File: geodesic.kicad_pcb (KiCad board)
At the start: 2 copper layers, 127.7 x 130 mm, 12 parts, among them J2 Base, U1 ATtiny24A-MU

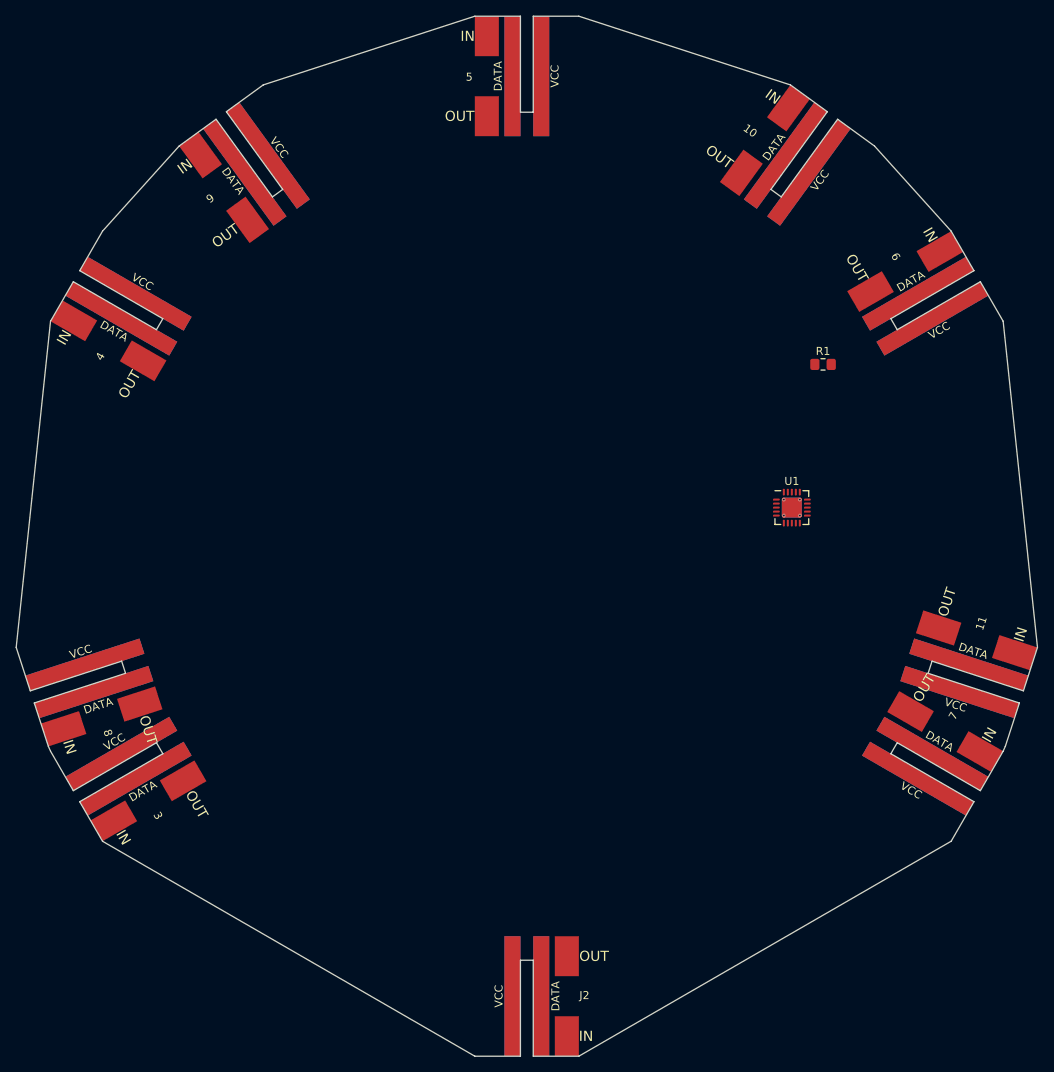
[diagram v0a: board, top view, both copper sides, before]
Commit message: Fixed out line and reduced diameter
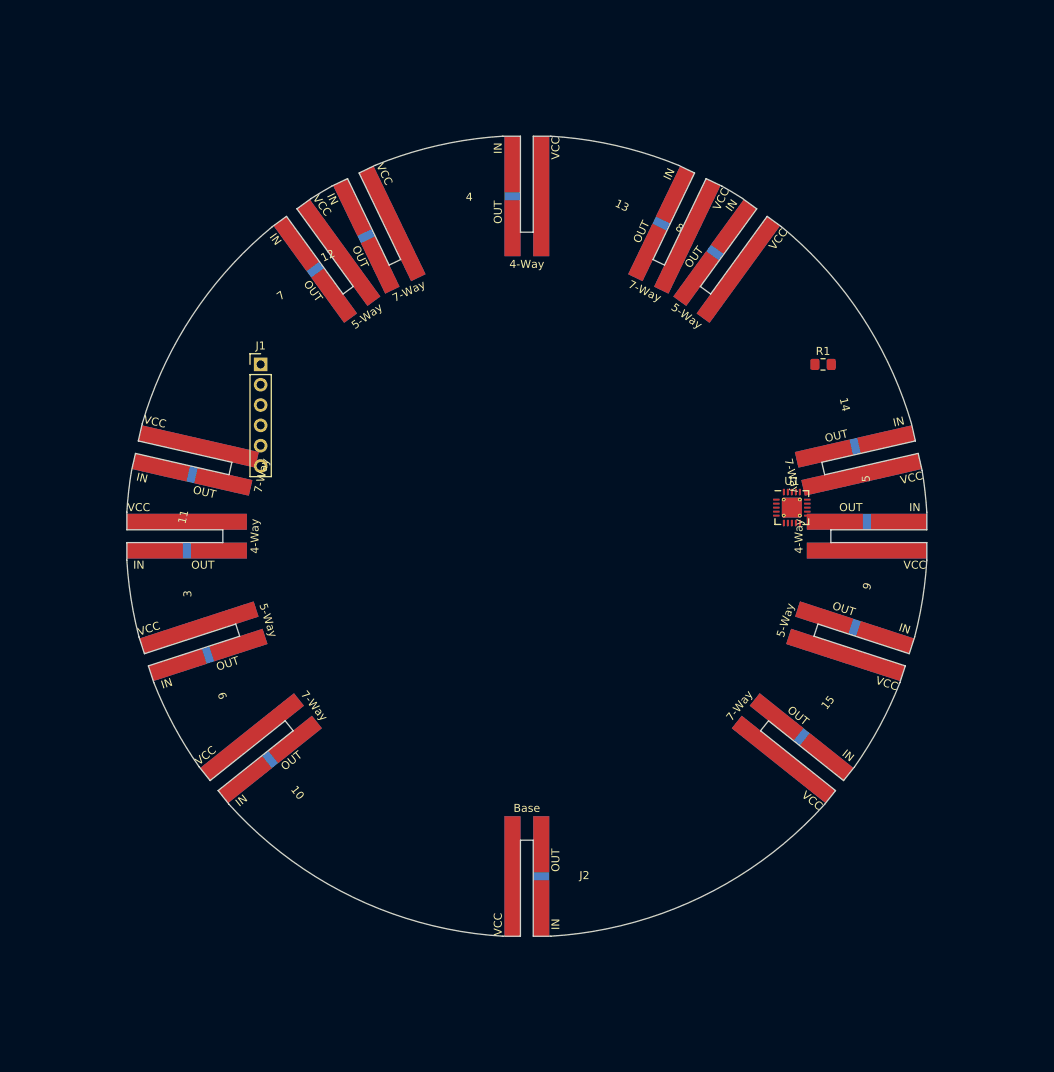
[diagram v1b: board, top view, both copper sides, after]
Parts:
- added 12: 7-Way, local:Geodesic_Hub_Connector, F.Cu at (126.3, 60.0)
- added 13: 7-Way, local:Geodesic_Hub_Connector, F.Cu at (169.7, 60.0)
- added 14: 7-Way, local:Geodesic_Hub_Connector, F.Cu at (196.8, 93.9)
- added 15: 7-Way, local:Geodesic_Hub_Connector, F.Cu at (187.1, 136.2)
- added J1: Program, Connector_PinHeader_2.54mm:PinHeader_1x06_P2.54mm_Vertical, F.Cu at (114.7, 83.5)
- 10, 11: value Pentagon -> 7-Way
- 3, 4, 5: value Hexagon -> 4-Way
- 6, 7: value Hexagon -> 5-Way
- 8, 9: value Pentagon -> 5-Way
- moved 11 114.9 mm to (99.2, 93.9), turned to 257.14 degrees
- moved 6 114.4 mm to (100.5, 120.5), turned to 288 degrees
- moved 10 114.0 mm to (108.9, 136.2), turned to 308.57 degrees
- moved 7 112.5 mm to (118.6, 64.5), turned to 216 degrees
- moved 8 109.5 mm to (177.4, 64.5), turned to 144 degrees
- moved 9 109.5 mm to (195.6, 120.5), turned to 72 degrees
- moved 5 82.0 mm to (198.0, 105.0), turned to 90 degrees
- moved 4 58.9 mm to (148.0, 55.0), turned to 180 degrees
- moved 3 33.1 mm to (98.0, 105.0), turned to 270 degrees
- moved J2 15.0 mm to (148.0, 155.0)
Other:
- board size 127.7 x 130 mm -> 100 x 100 mm

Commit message: Added spoke connector
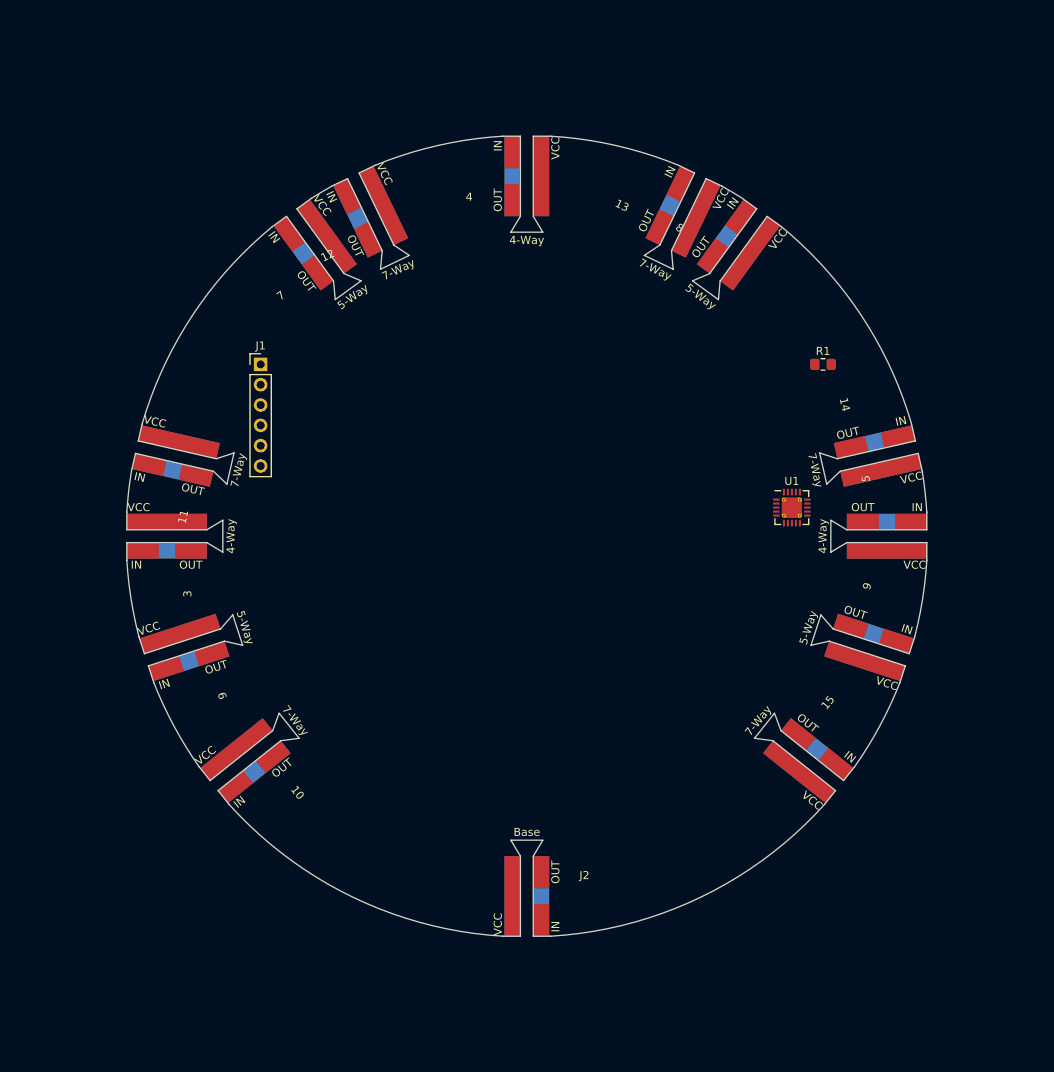
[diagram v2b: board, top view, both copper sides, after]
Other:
- outline, holes or cut-outs redrawn

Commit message: Exported step files
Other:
- outline, holes or cut-outs redrawn

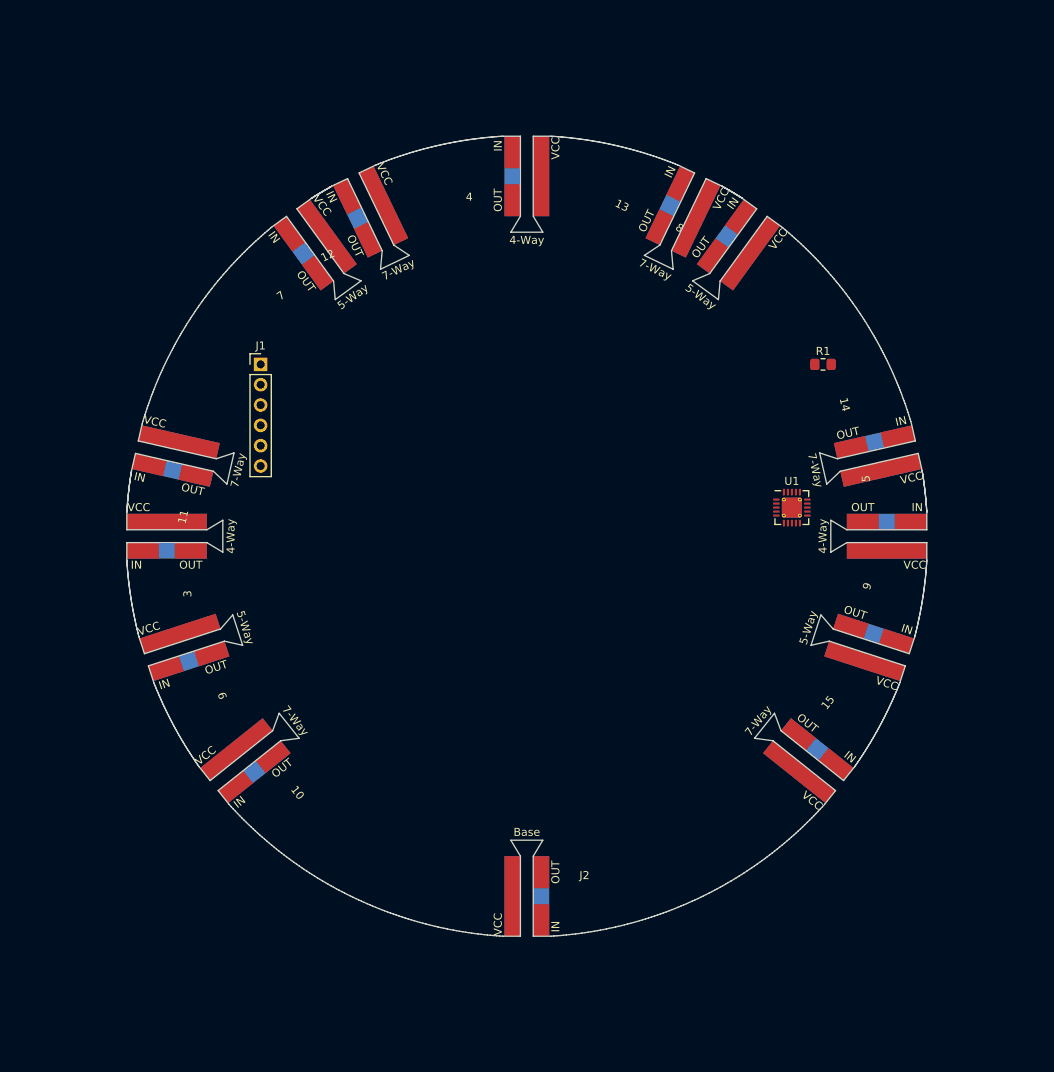
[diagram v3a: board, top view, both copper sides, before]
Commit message: Now with the proper angles
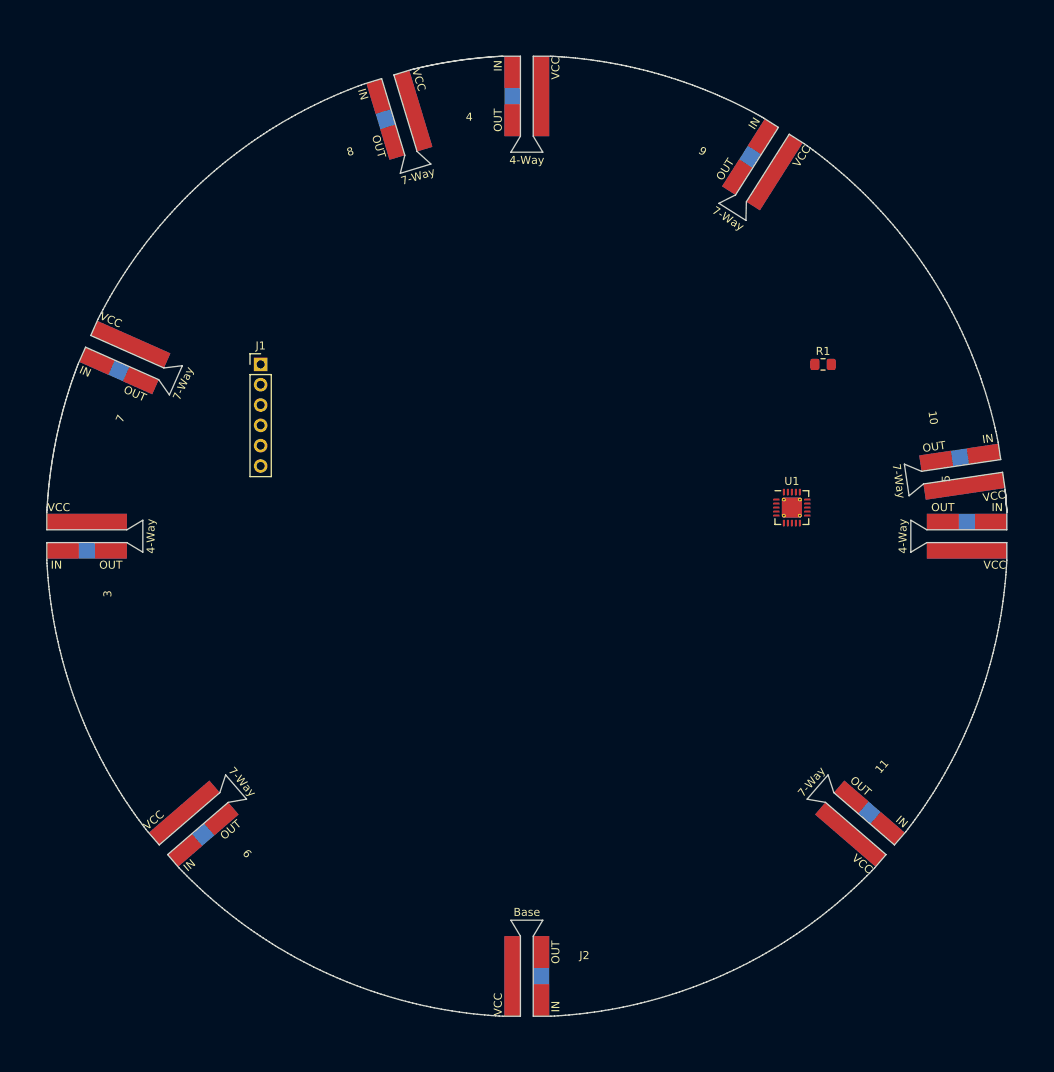
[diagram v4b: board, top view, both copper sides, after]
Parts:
- removed 12, 13, 14, 15: 7-Way, local:Geodesic_Hub_Connector
- 6, 7, 8, 9: value 5-Way -> 7-Way
- moved 11 106.8 mm to (193.4, 144.2), turned to 49.21 degrees
- moved 10 106.2 mm to (207.3, 96.2), turned to 98.42 degrees
- moved 9 67.9 mm to (180.1, 54.3), turned to 147.63 degrees
- moved 8 49.8 mm to (130.6, 47.6), turned to 196.84 degrees
- moved 7 30.1 mm to (93.2, 80.6), turned to 246.05 degrees
- moved 6 23.8 mm to (102.6, 144.2), turned to 310.79 degrees
- moved 3 10.0 mm to (88.0, 105.0)
- moved 4 10.0 mm to (148.0, 45.0)
- moved 5 10.0 mm to (208.0, 105.0)
- moved J2 10.0 mm to (148.0, 165.0)
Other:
- board size 100 x 100 mm -> 120 x 120 mm

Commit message: Layed out pcb
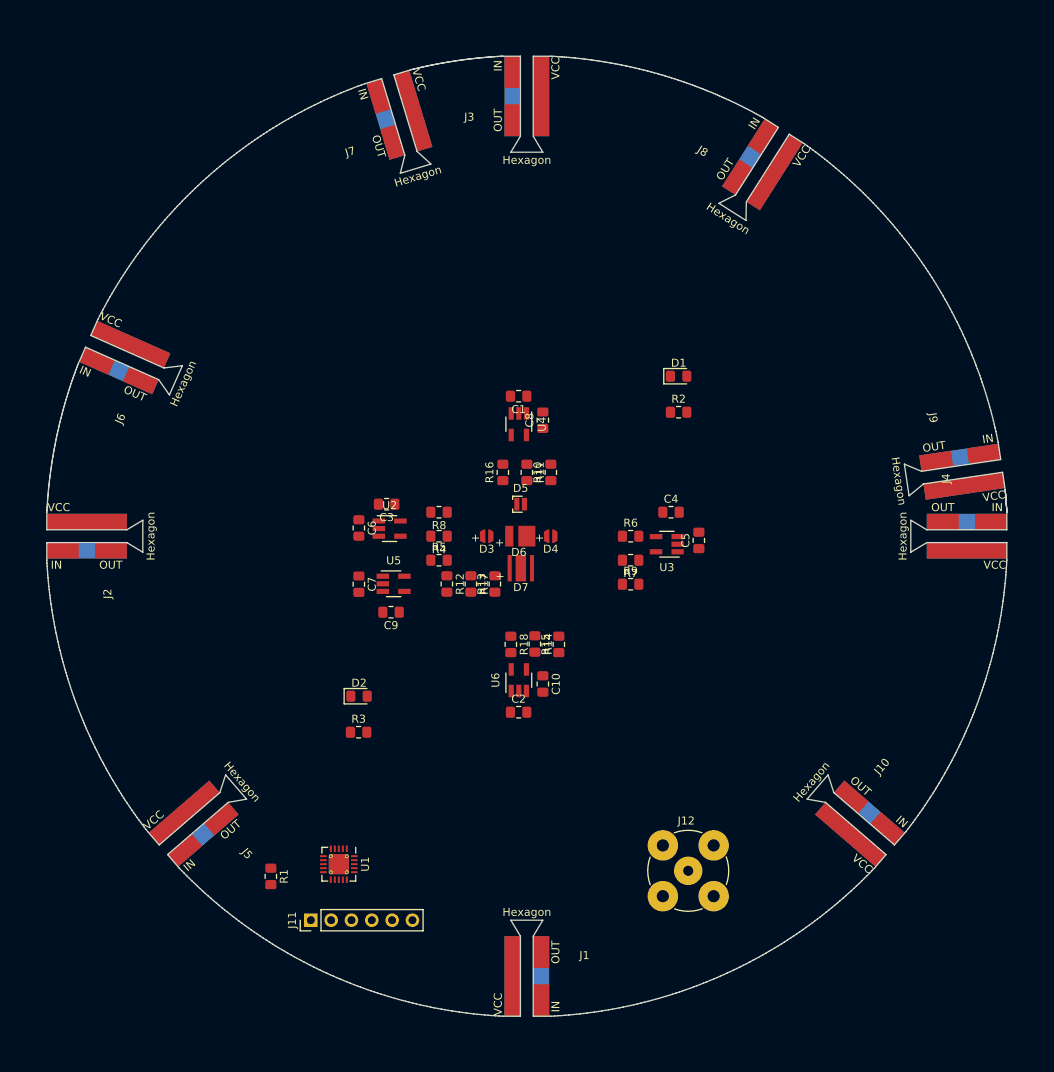
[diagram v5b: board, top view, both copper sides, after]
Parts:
- removed 10, 11, 6, 7, 8, 9: 7-Way, local:Geodesic_Hub_Connector
- removed 3, 4, 5: 4-Way, local:Geodesic_Hub_Connector
- added C1: 1uF, Capacitor_SMD:C_0805_2012Metric_Pad1.15x1.40mm_HandSolder, F.Cu at (147.0, 87.5)
- added C10: 2.2uF, Capacitor_SMD:C_0805_2012Metric_Pad1.15x1.40mm_HandSolder, F.Cu at (150.0, 123.5)
- added C2: 1uF, Capacitor_SMD:C_0805_2012Metric_Pad1.15x1.40mm_HandSolder, F.Cu at (147.0, 127.0)
- added C3: 2.2uF, Capacitor_SMD:C_0805_2012Metric_Pad1.15x1.40mm_HandSolder, F.Cu at (130.5, 101.0)
- added C4: 2.2uF, Capacitor_SMD:C_0805_2012Metric_Pad1.15x1.40mm_HandSolder, F.Cu at (166.0, 102.0)
- added C5: 1uF, Capacitor_SMD:C_0805_2012Metric_Pad1.15x1.40mm_HandSolder, F.Cu at (169.5, 105.5)
- added C6: 1uF, Capacitor_SMD:C_0805_2012Metric_Pad1.15x1.40mm_HandSolder, F.Cu at (127.0, 104.0)
- added C7: 1uF, Capacitor_SMD:C_0805_2012Metric_Pad1.15x1.40mm_HandSolder, F.Cu at (127.0, 111.0)
- added C8: 2.2uF, Capacitor_SMD:C_0805_2012Metric_Pad1.15x1.40mm_HandSolder, F.Cu at (150.0, 90.5)
- added C9: 2.2uF, Capacitor_SMD:C_0805_2012Metric_Pad1.15x1.40mm_HandSolder, F.Cu at (131.0, 114.5)
- added D1: LED, LED_SMD:LED_0805_2012Metric_Pad1.15x1.40mm_HandSolder, F.Cu at (167.0, 85.0)
- added D2: LED, LED_SMD:LED_0805_2012Metric_Pad1.15x1.40mm_HandSolder, F.Cu at (127.0, 125.0)
- added D3: LED, local:XNOVA MP1616, F.Cu at (143.0, 105.0)
- added D4: LED, local:XNOVA MP1616, F.Cu at (151.0, 105.0)
- added D5: LED, LED_SMD:LED_Cree-XQ, F.Cu at (147.2, 101.0)
- added D6: LED, local:LUXEON_3535L, F.Cu at (147.0, 105.0)
- added D7: LED, local:Cree_XPE, F.Cu at (147.2, 109.0)
- added J1: Hexagon, local:Geodesic_Hub_Connector, F.Cu at (148.0, 165.0)
- added J10: Hexagon, local:Geodesic_Hub_Connector, F.Cu at (193.4, 144.2)
- added J12: AudioJack2_Ground, Connector_Coaxial:BNC_TEConnectivity_1478204_Vertical, F.Cu at (168.2, 146.8)
- added J3: Hexagon, local:Geodesic_Hub_Connector, F.Cu at (148.0, 45.0)
- added J4: Hexagon, local:Geodesic_Hub_Connector, F.Cu at (208.0, 105.0)
- added J5: Hexagon, local:Geodesic_Hub_Connector, F.Cu at (102.6, 144.2)
- added J6: Hexagon, local:Geodesic_Hub_Connector, F.Cu at (93.2, 80.6)
- added J7: Hexagon, local:Geodesic_Hub_Connector, F.Cu at (130.6, 47.6)
- added J8: Hexagon, local:Geodesic_Hub_Connector, F.Cu at (180.1, 54.3)
- added J9: Hexagon, local:Geodesic_Hub_Connector, F.Cu at (207.3, 96.2)
- added R10: R, Resistor_SMD:R_0805_2012Metric_Pad1.15x1.40mm_HandSolder, F.Cu at (151.0, 97.0)
- added R11: R, Resistor_SMD:R_0805_2012Metric_Pad1.15x1.40mm_HandSolder, F.Cu at (148.0, 97.0)
- added R12: R, Resistor_SMD:R_0805_2012Metric_Pad1.15x1.40mm_HandSolder, F.Cu at (138.0, 111.0)
- added R13: R, Resistor_SMD:R_0805_2012Metric_Pad1.15x1.40mm_HandSolder, F.Cu at (144.0, 111.0)
- added R14: R, Resistor_SMD:R_0805_2012Metric_Pad1.15x1.40mm_HandSolder, F.Cu at (149.0, 118.5)
- added R15: R, Resistor_SMD:R_0805_2012Metric_Pad1.15x1.40mm_HandSolder, F.Cu at (152.0, 118.5)
- added R16: R, Resistor_SMD:R_0805_2012Metric_Pad1.15x1.40mm_HandSolder, F.Cu at (145.0, 97.0)
- added R17: R, Resistor_SMD:R_0805_2012Metric_Pad1.15x1.40mm_HandSolder, F.Cu at (141.0, 111.0)
- added R18: R, Resistor_SMD:R_0805_2012Metric_Pad1.15x1.40mm_HandSolder, F.Cu at (146.0, 118.5)
- added R2: R, Resistor_SMD:R_0805_2012Metric_Pad1.15x1.40mm_HandSolder, F.Cu at (167.0, 89.5)
- added R3: R, Resistor_SMD:R_0805_2012Metric_Pad1.15x1.40mm_HandSolder, F.Cu at (127.0, 129.5)
- added R4: R, Resistor_SMD:R_0805_2012Metric_Pad1.15x1.40mm_HandSolder, F.Cu at (137.0, 105.0)
- added R5: R, Resistor_SMD:R_0805_2012Metric_Pad1.15x1.40mm_HandSolder, F.Cu at (137.0, 108.0)
- added R6: R, Resistor_SMD:R_0805_2012Metric_Pad1.15x1.40mm_HandSolder, F.Cu at (161.0, 105.0)
- added R7: R, Resistor_SMD:R_0805_2012Metric_Pad1.15x1.40mm_HandSolder, F.Cu at (161.0, 108.0)
- added R8: R, Resistor_SMD:R_0805_2012Metric_Pad1.15x1.40mm_HandSolder, F.Cu at (137.0, 102.0)
- added R9: R, Resistor_SMD:R_0805_2012Metric_Pad1.15x1.40mm_HandSolder, F.Cu at (161.0, 111.0)
- added U2: PAM2800, Package_TO_SOT_SMD:SOT-23-5_HandSoldering, F.Cu at (130.8, 104.0)
- added U3: PAM2800, Package_TO_SOT_SMD:SOT-23-5_HandSoldering, F.Cu at (165.5, 106.0)
- added U4: PAM2800, Package_TO_SOT_SMD:SOT-23-5_HandSoldering, F.Cu at (147.0, 91.0)
- added U5: PAM2800, Package_TO_SOT_SMD:SOT-23-5_HandSoldering, F.Cu at (131.3, 111.0)
- added U6: PAM2800, Package_TO_SOT_SMD:SOT-23-5_HandSoldering, F.Cu at (147.0, 123.0)
- J2: value Base -> Hexagon
- moved R1 94.1 mm to (116.0, 147.5), turned to 270 degrees
- moved J2 84.9 mm to (88.0, 105.0), turned to 270 degrees
- moved U1 72.1 mm to (124.5, 146.0), turned to 270 degrees
- moved J11 69.8 mm to (121.0, 153.0), turned to 90 degrees
- renumbered J1 to J11

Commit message: Added gerbers
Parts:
- moved U1 9.88 mm to (132.6, 140.4)
- moved R1 8.73 mm to (124.0, 151.0), turned to 90 degrees
- moved J11 3.61 mm to (124.0, 155.0)
- turned J10 to 49 degrees
- turned J5 to 311 degrees
- turned J6 to 246 degrees
- turned J7 to 197 degrees
- turned J8 to 148 degrees
- turned J9 to 98 degrees
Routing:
- net +5V: track 0.00 -> 605.8 mm, vias 0 -> 28
- net GND: track 0.00 -> 550.4 mm, vias 0 -> 14
- net /Clock: track 0.00 -> 434.6 mm, vias 0 -> 3
- net /Data_In: track 0.00 -> 427.9 mm, vias 0 -> 5
- net /Data_Out: track 0.00 -> 358.9 mm, vias 0 -> 14
- net Net-(R2-Pad1): track 0.00 -> 79.0 mm, vias 0 -> 2
- net Net-(U1-Pad4): track 0.00 -> 67.9 mm, vias 0 -> 2
- net Net-(U1-Pad3): track 0.00 -> 58.0 mm, vias 0 -> 2
- net Net-(U1-Pad5): track 0.00 -> 39.2 mm, vias 0 -> 2
- net Net-(U1-Pad15): track 0.00 -> 35.2 mm, vias 0 -> 2
- net /Reset: track 0.00 -> 32.2 mm, vias 0 -> 1
- net Net-(U1-Pad2): track 0.00 -> 28.7 mm
- net Net-(C9-Pad1): track 0.00 -> 28.5 mm
- net Net-(R3-Pad1): track 0.00 -> 26.6 mm
- net Net-(C10-Pad1): track 0.00 -> 24.9 mm
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- added copper zone on F.Cu, net +5V
- added copper zone on B.Cu, net GND
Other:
- net class Default: clearance 0.2 -> 0.15; trace_width 0.25 -> 0.2
- rule trace_clearance: 0.2 -> 0.15
- rule trace_min: 0.2 -> 0.1
